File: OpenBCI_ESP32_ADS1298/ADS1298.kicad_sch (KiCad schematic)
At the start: 35 parts, among them J2 Conn_02x08_Odd_Even, J3 Conn_02x03_Odd_Even, J4 Conn_02x02_Odd_Even, J5 Conn_01x02, J6 Conn_01x02, J7 Conn_01x02, U7 ADS1298RIZXGR

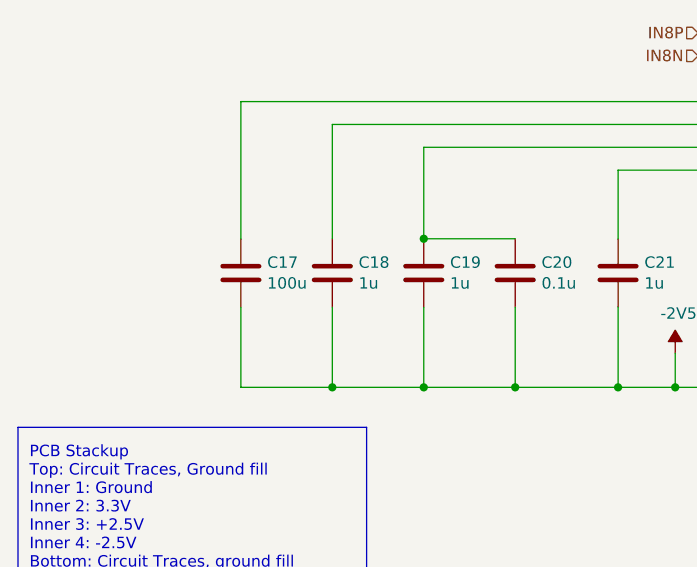
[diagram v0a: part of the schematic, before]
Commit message: Update footprints
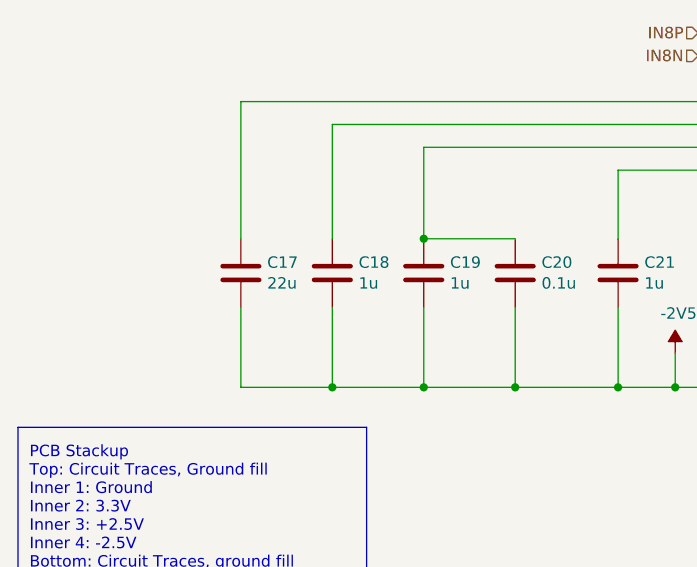
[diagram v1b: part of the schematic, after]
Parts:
- C17: value 100u -> 22u; footprint Capacitor_SMD:C_1210_3225Metric -> Capacitor_SMD:C_0805_2012Metric
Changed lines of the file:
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@@
       (effects (font (size 1.27 1.27)) (justify left))
     )
-    (property "Value" "100u" (at 48.641 137.033 0)
+    (property "Value" "22u" (at 48.641 137.033 0)
       (effects (font (size 1.27 1.27)) (justify left))
     )
-    (property "Footprint" "Capacitor_SMD:C_1210_3225Metric" (at 46.6852 139.7 0)
+    (property "Footprint" "Capacitor_SMD:C_0805_2012Metric" (at 46.6852 139.7 0)
       (effects (font (size 1.27 1.27)) hide)
     )

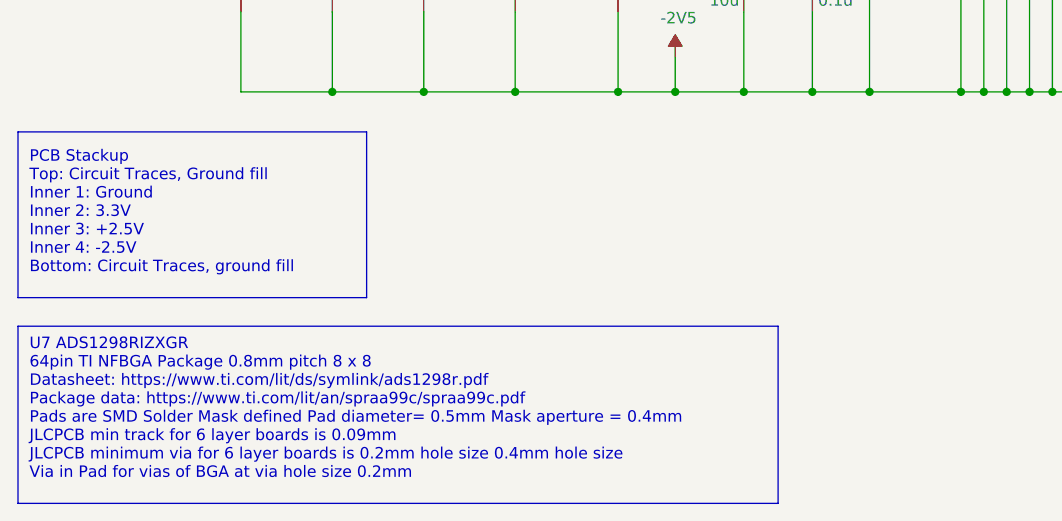
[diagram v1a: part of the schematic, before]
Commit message: Changes to meet JLCPCB Rules
Change BGA pad size and track routing. Change Via size to lower cost
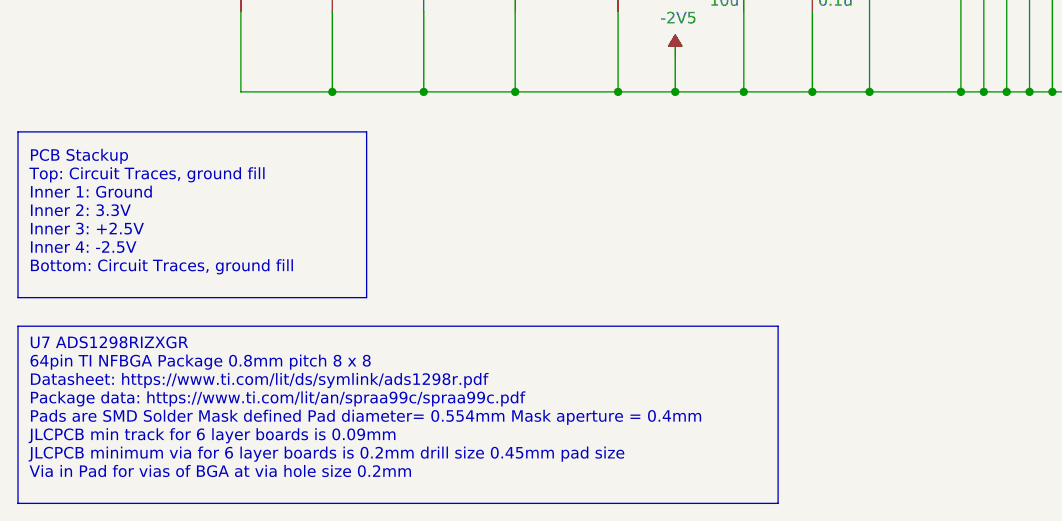
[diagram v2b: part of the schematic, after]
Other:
- note added: "PCB Stackup Top: Circuit Traces, ground fill Inner 1: Ground Inner 2: 3.3V Inner 3: +2.5V Inner 4: -2.5V Bottom: Circuit Traces, ground fill"
- note added: "U7 ADS1298RIZXGR 64pin TI NFBGA Package 0.8mm pitch 8 x 8 Datasheet: https://www.ti.com/lit/ds/symlink/ads1298r.pdf Package data: https://www.ti.com/lit/an/spraa99c/spraa99c.pdf Pads are SMD Solder Mask defined Pad diameter= 0.554mm Mask aperture = 0.4mm JLCPCB min track for 6 layer boards is 0.09mm JLCPCB minimum via for 6 layer boards is 0.2mm drill size 0.45mm pad size Via in Pad for vias of B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"
- note removed: "PCB Stackup Top: Circuit Traces, Ground fill Inner 1: Ground Inner 2: 3.3V Inner 3: +2.5V Inner 4: -2.5V Bottom: Circuit Traces, ground fill"
- note removed: "U7 ADS1298RIZXGR 64pin TI NFBGA Package 0.8mm pitch 8 x 8 Datasheet: https://www.ti.com/lit/ds/symlink/ads1298r.pdf Package data: https://www.ti.com/lit/an/spraa99c/spraa99c.pdf Pads are SMD Solder Mask defined Pad diameter= 0.5mm Mask aperture = 0.4mm JLCPCB min track for 6 layer boards is 0.09mm JLCPCB minimum via for 6 layer boards is 0.2mm hole size 0.4mm hole size Via in Pad for vias of BGA 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"
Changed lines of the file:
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@@
     (effects (font (size 1.27 1.27)) (justify left bottom))
   )
-  (text "U7 ADS1298RIZXGR\n64pin TI NFBGA Package 0.8mm pitch 8 x 8\nDatasheet: https://www.ti.com/lit/ds/symlink/ads1298r.pdf\nPackage data: https://www.ti.com/lit/an/spraa99c/spraa99c.pdf\nPads are SMD Solder Mask defined Pad diameter= 0.5mm Mask aperture = 0.4mm\nJLCPCB min track for 6 layer boards is 0.09mm\nJLCPCB minimum via for 6 layer boards is 0.2mm hole size 0.4mm hole size\nVia in Pad for vias of BGA at via hole size 0.2mm"
+  (text "U7 ADS1298RIZXGR\n64pin TI NFBGA Package 0.8mm pitch 8 x 8\nDatasheet: https://www.ti.com/lit/ds/symlink/ads1298r.pdf\nPackage data: https://www.ti.com/lit/an/spraa99c/spraa99c.pdf\nPads are SMD Solder Mask defined Pad diameter= 0.554mm Mask aperture = 0.4mm\nJLCPCB min track for 6 layer boards is 0.09mm\nJLCPCB minimum via for 6 layer boards is 0.2mm drill size 0.45mm pad size\nVia in Pad for vias of BGA at via hole size 0.2mm"
     (at 22.225 191.77 0)
     (effects (font (size 1.27 1.27)) (justify left bottom))
   )
-  (text "PCB Stackup\nTop: Circuit Traces, Ground fill\nInner 1: Ground\nInner 2: 3.3V\nInner 3: +2.5V\nInner 4: -2.5V\nBottom: Circuit Traces, ground fill"
+  (text "PCB Stackup\nTop: Circuit Traces, ground fill\nInner 1: Ground\nInner 2: 3.3V\nInner 3: +2.5V\nInner 4: -2.5V\nBottom: Circuit Traces, ground fill"
     (at 22.225 168.91 0)
     (effects (font (size 1.27 1.27)) (justify left bottom))
